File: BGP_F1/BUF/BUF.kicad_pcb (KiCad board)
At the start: 2 copper layers, 28 x 24 mm, 21 parts, among them P1 CONN_01X02, P2 CONN_01X05, P3 CONN_01X12, U1 MC33178

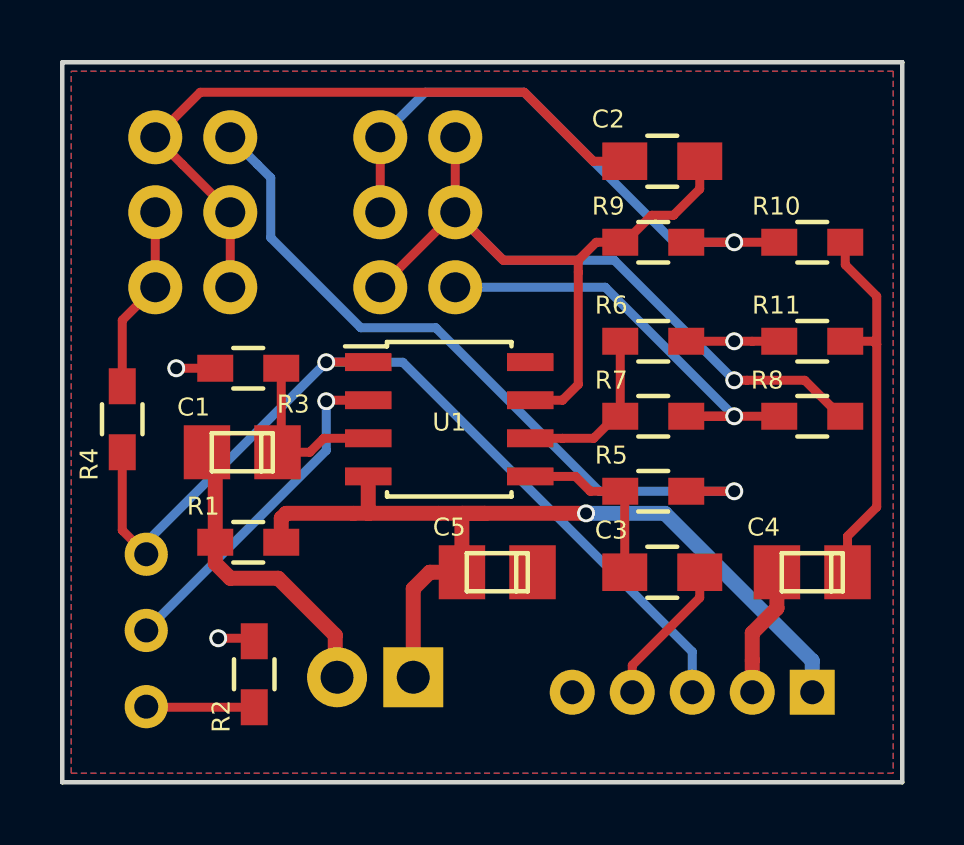
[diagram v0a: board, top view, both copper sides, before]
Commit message: F boards routed, various optimisations made
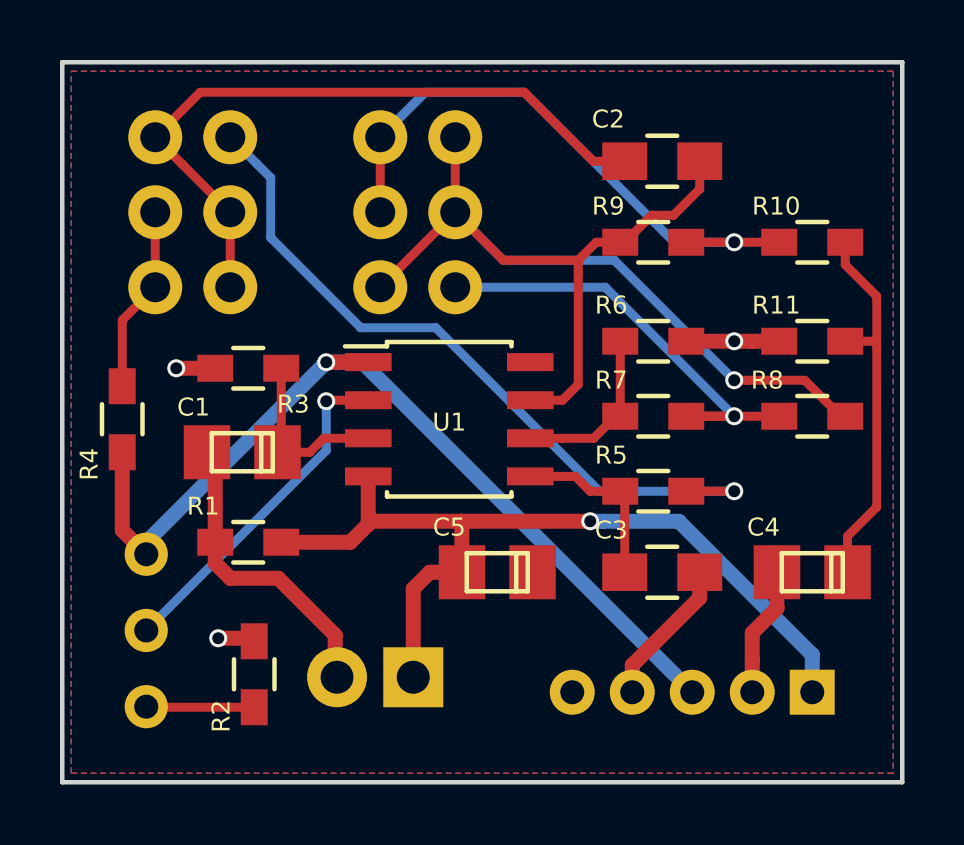
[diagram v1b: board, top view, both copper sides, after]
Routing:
- net Earth: track 30.6 -> 29.3 mm
- net /BUF_O: track 31.6 -> 30.8 mm
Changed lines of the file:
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@@
     (thickness 1.6)
     (drawings 8)
-    (tracks 141)
+    (tracks 140)
     (zones 0)
     (modules 21)
@@
   (segment (start 149.75 93) (end 149.75 90.45) (width 0.3) (layer F.Cu) (net 5))
   (segment (start 149.75 90.45) (end 149.6 90.3) (width 0.3) (layer F.Cu) (net 5))
-  (segment (start 150 97) (end 150 96.1) (width 0.3) (layer F.Cu) (net 6))
-  (segment (start 150 96.1) (end 152.25 93.85) (width 0.3) (layer F.Cu) (net 6))
-  (segment (start 152.25 93.85) (end 152.25 93) (width 0.3) (layer F.Cu) (net 6))
-  (segment (start 137.4 95.3) (end 137.3 95.3) (width 0.3) (layer F.Cu) (net 6))
-  (segment (start 137.3 95.3) (end 137.2 95.2) (width 0.3) (layer F.Cu) (net 6))
-  (segment (start 137.2 95.2) (end 136.199996 95.2) (width 0.3) (layer F.Cu) (net 6))
+  (segment (start 150 97) (end 150 96.1) (width 0.5) (layer F.Cu) (net 6))
+  (segment (start 150 96.1) (end 152.25 93.85) (width 0.5) (layer F.Cu) (net 6))
+  (segment (start 152.25 93.85) (end 152.25 93) (width 0.5) (layer F.Cu) (net 6))
+  (segment (start 137.4 95.3) (end 137.3 95.3) (width 0.5) (layer F.Cu) (net 6))
+  (segment (start 137.3 95.3) (end 137.2 95.2) (width 0.5) (layer F.Cu) (net 6))
+  (segment (start 137.2 95.2) (end 136.199996 95.2) (width 0.5) (layer F.Cu) (net 6))
   (via (at 136.199996 95.2) (size 0.6) (drill 0.4) (layers F.Cu B.Cu) (net 6))
-  (segment (start 136.1 86.2) (end 134.8 86.2) (width 0.3) (layer F.Cu) (net 6))
+  (segment (start 136.1 86.2) (end 134.8 86.2) (width 0.5) (layer F.Cu) (net 6))
   (via (at 134.8 86.2) (size 0.6) (drill 0.4) (layers F.Cu B.Cu) (net 6))
-  (segment (start 153.4 85.3) (end 153.400002 85.3) (width 0.3) (layer F.Cu) (net 6))
+  (segment (start 153.4 85.3) (end 153.400002 85.3) (width 0.5) (layer F.Cu) (net 6))
   (via (at 153.400002 85.3) (size 0.6) (drill 0.4) (layers F.Cu B.Cu) (net 6))
-  (segment (start 153.4 85.3) (end 151.8 85.3) (width 0.3) (layer F.Cu) (net 6))
-  (segment (start 154 85.3) (end 153.4 85.3) (width 0.3) (layer F.Cu) (net 6))
-  (segment (start 154.9 85.3) (end 154 85.3) (width 0.3) (layer F.Cu) (net 6))
+  (segment (start 153.4 85.3) (end 151.8 85.3) (width 0.5) (layer F.Cu) (net 6))
+  (segment (start 154 85.3) (end 153.4 85.3) (width 0.5) (layer F.Cu) (net 6))
+  (segment (start 154.9 85.3) (end 154 85.3) (width 0.5) (layer F.Cu) (net 6))
   (segment (start 158.150001 83.800001) (end 158.150001 85.4) (width 0.3) (layer F.Cu) (net 7))
   (segment (start 158.150001 85.4) (end 158.150001 90.825589) (width 0.3) (layer F.Cu) (net 7))
@@
   (segment (start 154 95.02441) (end 154 95.93934) (width 0.5) (layer F.Cu) (net 8))
   (segment (start 154.82398 94.20043) (end 154 95.02441) (width 0.5) (layer F.Cu) (net 8))
+  (segment (start 141.2 91.4) (end 141.3 91.3) (width 0.5) (layer F.Cu) (net 9))
+  (segment (start 141.3 91.3) (end 144.299992 91.3) (width 0.5) (layer F.Cu) (net 9))
+  (segment (start 144.3 91.299992) (end 144.299992 91.3) (width 0.5) (layer F.Cu) (net 9))
+  (segment (start 138.3 92) (end 140.6 92) (width 0.5) (layer F.Cu) (net 9))
+  (segment (start 140.6 92) (end 141.2 91.4) (width 0.5) (layer F.Cu) (net 9))
+  (segment (start 141.2 91.4) (end 141.2 89.805) (width 0.5) (layer F.Cu) (net 9))
+  (segment (start 148.6 91.299992) (end 144.3 91.299992) (width 0.5) (layer F.Cu) (net 9))
+  (segment (start 144.32398 93) (end 144.32398 91.323972) (width 0.5) (layer F.Cu) (net 9))
+  (segment (start 144.32398 91.323972) (end 144.3 91.299992) (width 0.5) (layer F.Cu) (net 9))
+  (segment (start 156 95.75) (end 151.549992 91.299992) (width 0.5) (layer B.Cu) (net 9))
+  (segment (start 149.024264 91.299992) (end 148.6 91.299992) (width 0.5) (layer B.Cu) (net 9))
+  (segment (start 151.549992 91.299992) (end 149.024264 91.299992) (width 0.5) (layer B.Cu) (net 9))
+  (via (at 148.6 91.299992) (size 0.6) (drill 0.4) (layers F.Cu B.Cu) (net 9))
+  (segment (start 156 97) (end 156 95.75) (width 0.5) (layer B.Cu) (net 9))
   (segment (start 142.7 96.5) (end 142.7 93.54928) (width 0.5) (layer F.Cu) (net 9))
   (segment (start 143.24928 93) (end 144.32398 93) (width 0.5) (layer F.Cu) (net 9))
   (segment (start 142.7 93.54928) (end 143.24928 93) (width 0.5) (layer F.Cu) (net 9))
-  (segment (start 143.536786 91.036786) (end 141.2 91.036786) (width 0.5) (layer F.Cu) (net 9))
-  (segment (start 141.2 91.036786) (end 140.7 91.036786) (width 0.5) (layer F.Cu) (net 9))
-  (segment (start 141.2 89.805) (end 141.2 91.036786) (width 0.5) (layer F.Cu) (net 9))
-  (segment (start 140.7 91.036786) (end 138.463214 91.036786) (width 0.5) (layer F.Cu) (net 9))
-  (segment (start 138.463214 91.036786) (end 138.3 91.2) (width 0.5) (layer F.Cu) (net 9))
-  (segment (start 138.3 91.2) (end 138.3 92) (width 0.5) (layer F.Cu) (net 9))
-  (segment (start 145.086764 91.036786) (end 144.32398 91.036786) (width 0.5) (layer F.Cu) (net 9))
-  (segment (start 144.32398 91.036786) (end 144.32398 93) (width 0.5) (layer F.Cu) (net 9))
-  (segment (start 145.086764 91.036786) (end 143.536786 91.036786) (width 0.5) (layer F.Cu) (net 9))
-  (segment (start 148.459831 91.036786) (end 145.086764 91.036786) (width 0.5) (layer F.Cu) (net 9))
-  (segment (start 156 97) (end 156 95.95) (width 0.5) (layer B.Cu) (net 9))
-  (segment (start 151.086786 91.036786) (end 148.459831 91.036786) (width 0.5) (layer B.Cu) (net 9))
-  (segment (start 156 95.95) (end 151.086786 91.036786) (width 0.5) (layer B.Cu) (net 9))
-  (via (at 148.459831 91.036786) (size 0.6) (drill 0.4) (layers F.Cu B.Cu) (net 9))
   (segment (start 138.45 92) (end 138.3 92) (width 0.5) (layer F.Cu) (net 9))
-  (segment (start 139.8 86) (end 133.8 92) (width 0.3) (layer B.Cu) (net 10))
-  (segment (start 133.8 92.4) (end 133 91.6) (width 0.3) (layer F.Cu) (net 10))
-  (segment (start 133 91.6) (end 133 89) (width 0.3) (layer F.Cu) (net 10))
-  (segment (start 133.8 92) (end 133.8 92.4) (width 0.3) (layer B.Cu) (net 10))
-  (segment (start 152 97) (end 152 95.648542) (width 0.3) (layer B.Cu) (net 10))
-  (segment (start 152 95.648542) (end 142.351458 86) (width 0.3) (layer B.Cu) (net 10))
-  (segment (start 142.351458 86) (end 140.224264 86) (width 0.3) (layer B.Cu) (net 10))
-  (segment (start 140.224264 86) (end 139.8 86) (width 0.3) (layer B.Cu) (net 10))
-  (segment (start 141.2 85.995) (end 139.805 85.995) (width 0.3) (layer F.Cu) (net 10))
-  (segment (start 139.805 85.995) (end 139.8 86) (width 0.3) (layer F.Cu) (net 10))
+  (segment (start 152 97) (end 141 86) (width 0.5) (layer B.Cu) (net 10))
+  (segment (start 141 86) (end 140.224264 86) (width 0.5) (layer B.Cu) (net 10))
+  (segment (start 140.224264 86) (end 139.8 86) (width 0.5) (layer B.Cu) (net 10))
+  (segment (start 139.8 86) (end 133.8 92) (width 0.5) (layer B.Cu) (net 10))
+  (segment (start 133.8 92.4) (end 133 91.6) (width 0.5) (layer F.Cu) (net 10))
+  (segment (start 133 91.6) (end 133 89) (width 0.5) (layer F.Cu) (net 10))
+  (segment (start 133.8 92) (end 133.8 92.4) (width 0.5) (layer B.Cu) (net 10))
+  (segment (start 141.2 85.995) (end 139.805 85.995) (width 0.5) (layer F.Cu) (net 10))
+  (segment (start 139.805 85.995) (end 139.8 86) (width 0.5) (layer F.Cu) (net 10))
   (via (at 139.8 86) (size 0.6) (drill 0.4) (layers F.Cu B.Cu) (net 10))
   (segment (start 134.1 83.5) (end 134.1 81) (width 0.3) (layer F.Cu) (net 12))

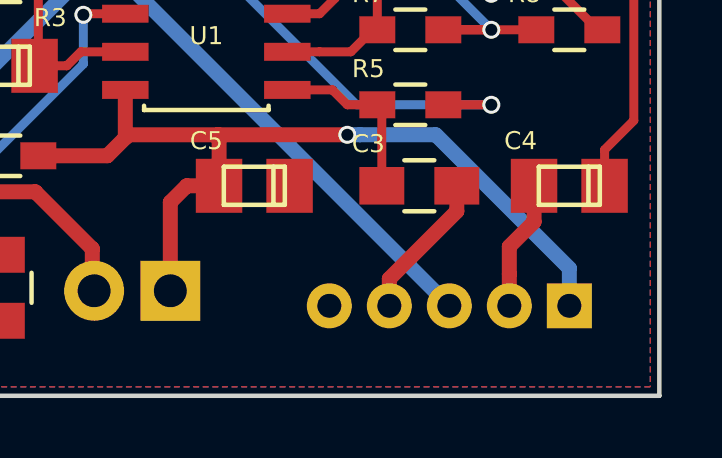
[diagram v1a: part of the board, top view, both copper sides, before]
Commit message: Flipped boards so that they should be facing the right way
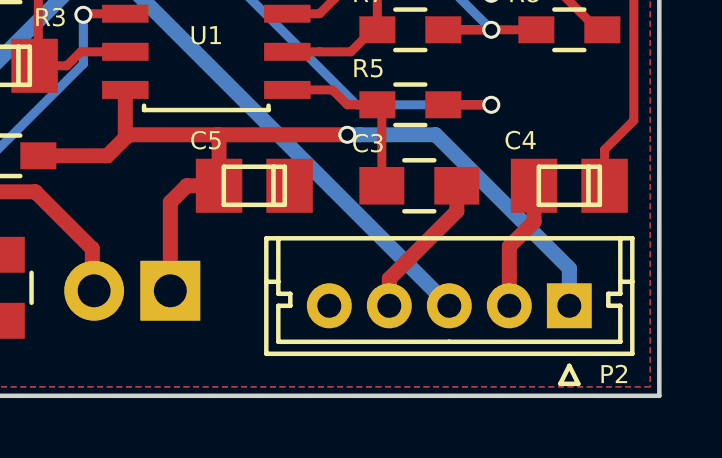
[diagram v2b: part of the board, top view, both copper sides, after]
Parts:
- P2: moved to F.Cu
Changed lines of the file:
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@@
     )
   )
-  (module Connectors_Molex:Molex_MicroLatch-53253-0570_05x2.00mm_Straight (layer B.Cu)
+  (module Connectors_Molex:Molex_MicroLatch-53253-0570_05x2.00mm_Straight (layer F.Cu)
     (at 156 97 180)
     (descr "Molex Micro-Latch connector, PN:53253-0570, top entry type, through hole")
     (tags "conn molex micro latch")
-    (fp_text reference P2 (at -1.5 2.3 180) (layer B.SilkS)
-      (effects (font (size 0.6 0.6) (thickness 0.15)) (justify mirror))
+    (fp_text reference P2 (at -1.5 -2.3 180) (layer F.SilkS)
+      (effects (font (size 0.6 0.6) (thickness 0.15)))
     )
-    (fp_text value CONN_01X05 (at 4 3.5 180) (layer B.Fab) hide
-      (effects (font (size 0.6 0.6) (thickness 0.15)) (justify mirror))
+    (fp_text value CONN_01X05 (at 4 -3.5 180) (layer F.Fab) hide
+      (effects (font (size 0.6 0.6) (thickness 0.15)))
     )
-    (fp_line (start -2.6 2.1) (end -2.6 -2.75) (layer B.CrtYd) (width 0.05))
-    (fp_line (start -2.6 -2.75) (end 10.55 -2.75) (layer B.CrtYd) (width 0.05))
-    (fp_line (start 10.55 -2.75) (end 10.55 2.1) (layer B.CrtYd) (width 0.05))
-    (fp_line (start 10.55 2.1) (end -2.6 2.1) (layer B.CrtYd) (width 0.05))
-    (fp_line (start -2.1 1.6) (end -2.1 -2.25) (layer B.SilkS) (width 0.15))
-    (fp_line (start -2.1 -2.25) (end 10.1 -2.25) (layer B.SilkS) (width 0.15))
-    (fp_line (start 10.1 -2.25) (end 10.1 1.6) (layer B.SilkS) (width 0.15))
-    (fp_line (start 10.1 1.6) (end -2.1 1.6) (layer B.SilkS) (width 0.15))
-    (fp_line (start 0 2) (end -0.3 2.6) (layer B.SilkS) (width 0.15))
-    (fp_line (start -0.3 2.6) (end 0.3 2.6) (layer B.SilkS) (width 0.15))
-    (fp_line (start 0.3 2.6) (end 0 2) (layer B.SilkS) (width 0.15))
-    (fp_line (start -2.1 -0.8) (end -1.7 -0.8) (layer B.SilkS) (width 0.15))
-    (fp_line (start 10.1 -0.8) (end 9.7 -0.8) (layer B.SilkS) (width 0.15))
-    (fp_line (start 4 1.2) (end -1.7 1.2) (layer B.SilkS) (width 0.15))
-    (fp_line (start -1.7 1.2) (end -1.7 0) (layer B.SilkS) (width 0.15))
-    (fp_line (start -1.7 0) (end -1.3 0) (layer B.SilkS) (width 0.15))
-    (fp_line (start -1.3 0) (end -1.3 -0.4) (layer B.SilkS) (width 0.15))
-    (fp_line (start -1.3 -0.4) (end -1.7 -0.4) (layer B.SilkS) (width 0.15))
-    (fp_line (start -1.7 -0.4) (end -1.7 -2.25) (layer B.SilkS) (width 0.15))
-    (fp_line (start 4 1.2) (end 9.7 1.2) (layer B.SilkS) (width 0.15))
-    (fp_line (start 9.7 1.2) (end 9.7 0) (layer B.SilkS) (width 0.15))
-    (fp_line (start 9.7 0) (end 9.3 0) (layer B.SilkS) (width 0.15))
-    (fp_line (start 9.3 0) (end 9.3 -0.4) (layer B.SilkS) (width 0.15))
-    (fp_line (start 9.3 -0.4) (end 9.7 -0.4) (layer B.SilkS) (width 0.15))
-    (fp_line (start 9.7 -0.4) (end 9.7 -2.25) (layer B.SilkS) (width 0.15))
+    (fp_line (start -2.6 -2.1) (end -2.6 2.75) (layer F.CrtYd) (width 0.05))
+    (fp_line (start -2.6 2.75) (end 10.55 2.75) (layer F.CrtYd) (width 0.05))
+    (fp_line (start 10.55 2.75) (end 10.55 -2.1) (layer F.CrtYd) (width 0.05))
+    (fp_line (start 10.55 -2.1) (end -2.6 -2.1) (layer F.CrtYd) (width 0.05))
+    (fp_line (start -2.1 -1.6) (end -2.1 2.25) (layer F.SilkS) (width 0.15))
+    (fp_line (start -2.1 2.25) (end 10.1 2.25) (layer F.SilkS) (width 0.15))
+    (fp_line (start 10.1 2.25) (end 10.1 -1.6) (layer F.SilkS) (width 0.15))
+    (fp_line (start 10.1 -1.6) (end -2.1 -1.6) (layer F.SilkS) (width 0.15))
+    (fp_line (start 0 -2) (end -0.3 -2.6) (layer F.SilkS) (width 0.15))
+    (fp_line (start -0.3 -2.6) (end 0.3 -2.6) (layer F.SilkS) (width 0.15))
+    (fp_line (start 0.3 -2.6) (end 0 -2) (layer F.SilkS) (width 0.15))
+    (fp_line (start -2.1 0.8) (end -1.7 0.8) (layer F.SilkS) (width 0.15))
+    (fp_line (start 10.1 0.8) (end 9.7 0.8) (layer F.SilkS) (width 0.15))
+    (fp_line (start 4 -1.2) (end -1.7 -1.2) (layer F.SilkS) (width 0.15))
+    (fp_line (start -1.7 -1.2) (end -1.7 0) (layer F.SilkS) (width 0.15))
+    (fp_line (start -1.7 0) (end -1.3 0) (layer F.SilkS) (width 0.15))
+    (fp_line (start -1.3 0) (end -1.3 0.4) (layer F.SilkS) (width 0.15))
+    (fp_line (start -1.3 0.4) (end -1.7 0.4) (layer F.SilkS) (width 0.15))
+    (fp_line (start -1.7 0.4) (end -1.7 2.25) (layer F.SilkS) (width 0.15))
+    (fp_line (start 4 -1.2) (end 9.7 -1.2) (layer F.SilkS) (width 0.15))
+    (fp_line (start 9.7 -1.2) (end 9.7 0) (layer F.SilkS) (width 0.15))
+    (fp_line (start 9.7 0) (end 9.3 0) (layer F.SilkS) (width 0.15))
+    (fp_line (start 9.3 0) (end 9.3 0.4) (layer F.SilkS) (width 0.15))
+    (fp_line (start 9.3 0.4) (end 9.7 0.4) (layer F.SilkS) (width 0.15))
+    (fp_line (start 9.7 0.4) (end 9.7 2.25) (layer F.SilkS) (width 0.15))
     (pad 1 thru_hole rect (at 0 0 180) (size 1.5 1.5) (drill 0.8) (layers *.Cu *.Mask)
       (net 9 Earth))

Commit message: Pot tinkering
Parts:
- turned C2 to 180 degrees
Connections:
- P3 pad 12: /PG1_1 -> /PG2_3
- P3 pad 2: /PF1_1 -> /PF1_2
- P3 pad 4: /PF1_3 -> /PF2_1
- P3 pad 9: /PG1_2 -> /PG1_3
- R4 pad 1: /PF1_1 -> /PF1_2
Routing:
- net /PF1_2: track 0.00 -> 6.46 mm
- net /PF1_1: track 6.26 -> 0.00 mm
- net /PG1_1: track 38.5 -> 34.6 mm
- net /PG1_2: track 20.2 -> 22.5 mm
- net /PF1_3: track 23.3 -> 23.8 mm
